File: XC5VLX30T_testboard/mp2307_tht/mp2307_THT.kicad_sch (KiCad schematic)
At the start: 13 parts, among them J1 Inductor L, J2 Inductor_R, J4 Conn_01x06_Pin, U1 MP2307DN-LF-Z

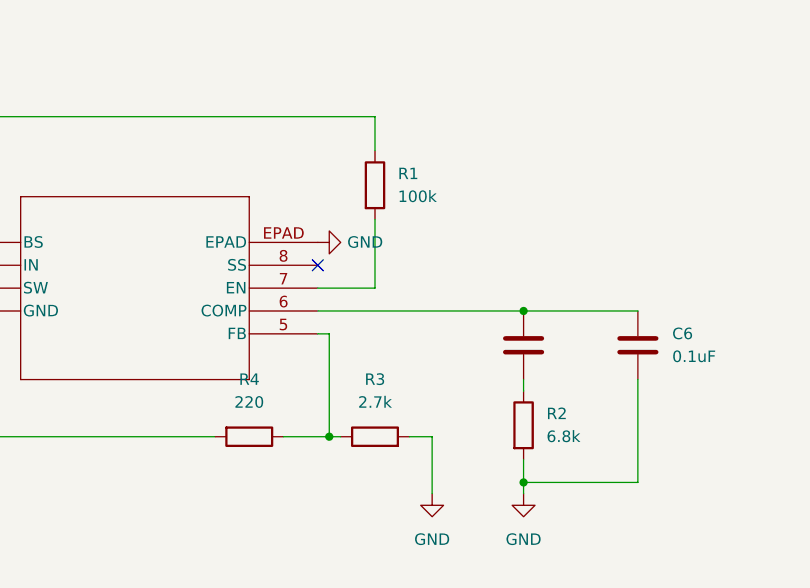
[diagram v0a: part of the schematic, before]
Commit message: update mp2307 tht resistor labels
resistor labels on mp2307 tht board now match datasheet
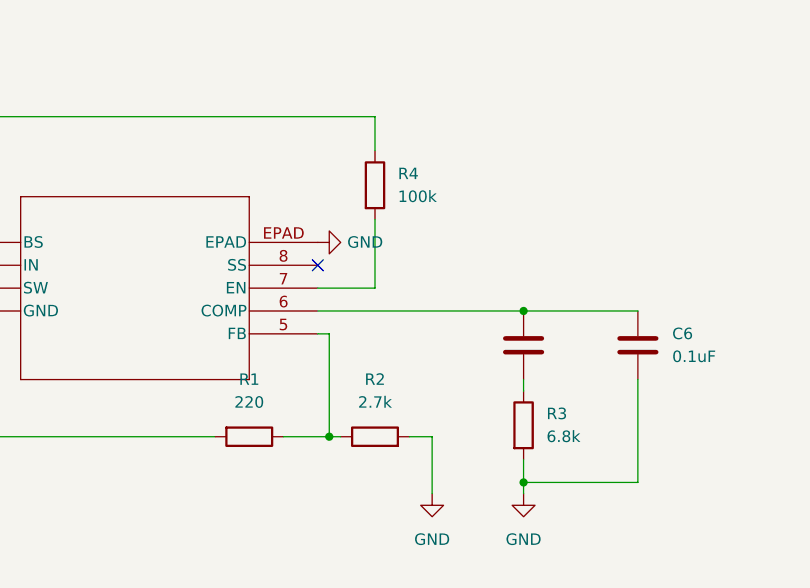
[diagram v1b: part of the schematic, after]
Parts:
- renumbered R4 to R1, R3 to R2, R2 to R3, R1 to R4
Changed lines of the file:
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@@
 		(dnp no)
 		(fields_autoplaced yes)
-		(property "Reference" "R3"
+		(property "Reference" "R2"
 			(at 175.26 88.9 90)
 			(effects
@@
 			(project ""
 				(path "/01e6d2e1-8ace-40fe-98d5-3b3fb62c000f"
-					(reference "R3")
+					(reference "R2")
 					(unit 1)
 				)
@@
 		(dnp no)
 		(fields_autoplaced yes)
-		(property "Reference" "R2"
+		(property "Reference" "R3"
 			(at 194.31 92.7099 0)
 			(effects
@@
 			(project ""
 				(path "/01e6d2e1-8ace-40fe-98d5-3b3fb62c000f"
-					(reference "R2")
+					(reference "R3")
 					(unit 1)
 				)
@@
 		(dnp no)
 		(fields_autoplaced yes)
-		(property "Reference" "R1"
+		(property "Reference" "R4"
 			(at 177.8 66.0399 0)
 			(effects
@@
 			(project ""
 				(path "/01e6d2e1-8ace-40fe-98d5-3b3fb62c000f"
-					(reference "R1")
+					(reference "R4")
 					(unit 1)
 				)
@@
 		(dnp no)
 		(fields_autoplaced yes)
-		(property "Reference" "R4"
+		(property "Reference" "R1"
 			(at 161.29 88.9 90)
 			(effects
@@
 			(project ""
 				(path "/01e6d2e1-8ace-40fe-98d5-3b3fb62c000f"
-					(reference "R4")
-					(unit 1)
-				)
+					(reference "R1")
+					(unit 1)
+				)
